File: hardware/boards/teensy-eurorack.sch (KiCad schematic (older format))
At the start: 101 parts, among them J1 Conn_01x08, J27 Conn_01x02, J28 Conn_02x08_Odd_Even, SW1 Rotary_Encoder_Switch, SW2 Rotary_Encoder_Switch, SW3 Rotary_Encoder_Switch, U1 CS42448, U2 AD5754BREZ, U3 AD5754BREZ, U4 Teensy4.1, U5 MCP1700-2502E_SOT23, U6 AD7606BSTZ, U7 6N138

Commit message: silkscreen
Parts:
- U5: value MCP1700-2502E_SOT23 -> MCP1700-2502E
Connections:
- net E1A: now also JB4.5 (Pin_5), JM4.5 (Pin_5); no longer JB4.7 (Pin_7), JM4.7 (Pin_7)
- net E1B: now also JB4.4 (Pin_4), JM4.4 (Pin_4); no longer JB4.6 (Pin_6), JM4.6 (Pin_6)
- net E2A: now also JB4.8 (Pin_8), JM4.8 (Pin_8); no longer JB4.5 (Pin_5), JM4.5 (Pin_5)
- net E2B: now also JB4.7 (Pin_7), JM4.7 (Pin_7); no longer JB4.4 (Pin_4), JM4.4 (Pin_4)
- net E3A: now also JB3.5 (Pin_5), JM3.5 (Pin_5); no longer JB4.3 (Pin_3), JM4.3 (Pin_3)
- net E3B: now also JB3.4 (Pin_4), JM3.4 (Pin_4); no longer JB4.2 (Pin_2), JM4.2 (Pin_2)
- net ES1: now also JB4.3 (Pin_3), JM4.3 (Pin_3); no longer JB3.3 (Pin_3), JM3.3 (Pin_3)
- net ES2: now also JB4.6 (Pin_6), JM4.6 (Pin_6); no longer JB3.2 (Pin_2), JM3.2 (Pin_2)
- net ES3: now also JB3.6 (Pin_6), JM3.6 (Pin_6); no longer JB4.8 (Pin_8), JM4.8 (Pin_8)
- net GND: now also JB3.7 (Pin_7), JM3.7 (Pin_7); no longer JB3.8 (Pin_8), JM3.8 (Pin_8)
- net P1: now also JB3.3 (Pin_3), JM3.3 (Pin_3); no longer JB3.7 (Pin_7), JM3.7 (Pin_7)
- net P2: now also JB3.2 (Pin_2), JM3.2 (Pin_2); no longer JB3.6 (Pin_6), JM3.6 (Pin_6)
- net P3: now also JB3.8 (Pin_8), JM3.8 (Pin_8); no longer JB3.5 (Pin_5), JM3.5 (Pin_5)
- net P4: now also JB4.2 (Pin_2), JM4.2 (Pin_2); no longer JB3.4 (Pin_4), JM3.4 (Pin_4)
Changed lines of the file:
@@
 P 13650 5950
 F 0 "U5" H 13500 5600 50  0000 L CNN
-F 1 "MCP1700-2502E_SOT23" H 12650 5700 50  0000 L CNN
+F 1 "MCP1700-2502E" H 12650 5700 50  0000 L CNN
 F 2 "Package_TO_SOT_SMD:SOT-23" H 13650 6175 50  0001 C CNN
 F 3 "http://ww1.microchip.com/downloads/en/DeviceDoc/20001826D.pdf" H 13650 5950 50  0001 C CNN
@@
 Wire Wire Line
 	14350 7350 14850 7350
+Text Label 14350 7150 0    49   ~ 0
+GND
+Text Label 14350 7550 0    49   ~ 0
+P1
+Text Label 14350 7650 0    49   ~ 0
+P2
 Text Label 14350 7050 0    49   ~ 0
-GND
-Text Label 14350 7150 0    49   ~ 0
-P1
-Text Label 14350 7250 0    49   ~ 0
-P2
-Text Label 14350 7350 0    49   ~ 0
 P3
 $Comp
@@
 Wire Wire Line
 	13100 7950 12150 7950
-Text Label 14350 7450 0    49   ~ 0
+Text Label 14500 9550 0    49   ~ 0
 P4
 Wire Wire Line
@@
 Wire Wire Line
 	14500 9650 15000 9650
-Text Label 14350 7550 0    49   ~ 0
+Text Label 14500 9450 0    49   ~ 0
 ES1
-Text Label 14350 7650 0    49   ~ 0
+Text Label 14500 9150 0    49   ~ 0
 ES2
+Text Label 14350 7250 0    49   ~ 0
+ES3
+Text Label 14500 9250 0    49   ~ 0
+E1A
+Text Label 14500 9350 0    49   ~ 0
+E1B
 Text Label 14500 8950 0    49   ~ 0
-ES3
+E2A
 Text Label 14500 9050 0    49   ~ 0
-E1A
-Text Label 14500 9150 0    49   ~ 0
-E1B
-Text Label 14500 9250 0    49   ~ 0
-E2A
-Text Label 14500 9350 0    49   ~ 0
 E2B
-Text Label 14500 9450 0    49   ~ 0
+Text Label 14350 7350 0    49   ~ 0
 E3A
-Text Label 14500 9550 0    49   ~ 0
+Text Label 14350 7450 0    49   ~ 0
 E3B
 $Comp

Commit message: silkscreen, corrections
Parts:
- added JBUSBA1, JBUSBB1: Conn_01x04, Connector_PinSocket_2.54mm:PinSocket_1x04_P2.54mm_Vertical, symbol Connector_Generic:Conn_01x04
- added JMUSBA1, JMUSBB1, JUSBA1, JUSBB1: Conn_01x04, Connector_PinHeader_2.54mm:PinHeader_1x04_P2.54mm_Vertical, symbol Connector_Generic:Conn_01x04
- added USBA1: USB-A-S-X-X-VT, footprints:USB-A-S-X-X-VT, symbol Connector_Generic:Conn_01x06
- added USBB1: 61400413321, footprints:WURTH_ELECTRONICS_61400413321_0, symbol Connector_Generic:Conn_01x06
- C12: value 4.7uF -> 4.7u
- C14: value 22uF -> 22u
- C16: value 100uF -> 100u
- C27, C29, C33, C34, C37: value 10uF -> 10u
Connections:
- net GND: now also JBUSBB1.1 (Pin_1), JMUSBB1.1 (Pin_1), JUSBB1.1 (Pin_1), USBB1.4 (Pin_4)
- new net: JBUSBA1.1 (Pin_1), JMUSBA1.1 (Pin_1), JUSBA1.1 (Pin_1), USBA1.4 (Pin_4)
- new net: JBUSBA1.2 (Pin_2), JMUSBA1.2 (Pin_2), JUSBA1.2 (Pin_2), USBA1.3 (Pin_3)
- new net: JBUSBA1.3 (Pin_3), JMUSBA1.3 (Pin_3), JUSBA1.3 (Pin_3), USBA1.2 (Pin_2)
- new net: JBUSBA1.4 (Pin_4), JMUSBA1.4 (Pin_4), JUSBA1.4 (Pin_4), USBA1.1 (Pin_1)
- new net: JBUSBB1.2 (Pin_2), JMUSBB1.2 (Pin_2), JUSBB1.2 (Pin_2), USBB1.3 (Pin_3)
- new net: JBUSBB1.3 (Pin_3), JMUSBB1.3 (Pin_3), JUSBB1.3 (Pin_3), USBB1.2 (Pin_2)
- new net: JBUSBB1.4 (Pin_4), JMUSBB1.4 (Pin_4), JUSBB1.4 (Pin_4), USBB1.1 (Pin_1)
- no-connect marks 32 -> 36
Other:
- moved on the sheet: JB1, JB2, JB3, JB4, JM1, JM2, JM3, JM4

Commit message: erc pass
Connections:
- net GND: now also U1.15 (DAC_SDIN3)
- no-connect marks 36 -> 63
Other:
- moved on the sheet: C42
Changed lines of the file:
@@
 L Device:C C42
 U 1 1 5EEE854A
-P 10200 7300
-F 0 "C42" V 10350 7300 50  0000 C CNN
-F 1 "10u" V 10050 7300 50  0000 C CNN
-F 2 "Capacitor_SMD:C_0805_2012Metric" H 10238 7150 50  0001 C CNN
-F 3 "~" H 10200 7300 50  0001 C CNN
-	1    10200 7300
+P 10800 7300
+F 0 "C42" V 10950 7300 50  0000 C CNN
+F 1 "10u" V 10650 7300 50  0000 C CNN
+F 2 "Capacitor_SMD:C_0805_2012Metric" H 10838 7150 50  0001 C CNN
+F 3 "~" H 10800 7300 50  0001 C CNN
+	1    10800 7300
 	0    1    1    0
 $EndComp
@@
 L power:GND #PWR0102
 U 1 1 5EEE9AAA
-P 10350 7300
-F 0 "#PWR0102" H 10350 7050 50  0001 C CNN
-F 1 "GND" H 10355 7127 50  0001 C CNN
-F 2 "" H 10350 7300 50  0001 C CNN
-F 3 "" H 10350 7300 50  0001 C CNN
-	1    10350 7300
+P 11100 7350
+F 0 "#PWR0102" H 11100 7100 50  0001 C CNN
+F 1 "GND" H 11105 7177 50  0001 C CNN
+F 2 "" H 11100 7350 50  0001 C CNN
+F 3 "" H 11100 7350 50  0001 C CNN
+	1    11100 7350
 	1    0    0    -1
 $EndComp
@@
 $EndComp
 NoConn ~ 14400 1650
-NoConn ~ 14350 1750
+NoConn ~ 14400 1750
 NoConn ~ 14400 4200
 NoConn ~ 14400 4300
@@
 F 3 "" H 12600 5950 50  0001 C CNN
 	1    12600 5950
-	0    -1   1    0
+	-1   0    0    -1
 $EndComp
 $Comp
@@
 	4850 6950 4950 6950
 Wire Wire Line
-	3150 5050 3150 5250
+	3150 5050 3150 5150
 Wire Wire Line
 	8250 6700 8250 6800
@@
 Wire Wire Line
 	14750 9150 14950 9150
+NoConn ~ 10150 3450
+NoConn ~ 10150 3250
+NoConn ~ 10150 2950
+NoConn ~ 10150 2850
+NoConn ~ 10150 2750
+NoConn ~ 7950 3450
+NoConn ~ 7950 3350
+NoConn ~ 7950 2550
+NoConn ~ 11750 7600
+NoConn ~ 11750 7500
+NoConn ~ 11750 7400
+NoConn ~ 12700 7400
+NoConn ~ 12700 7500
+NoConn ~ 12700 7600
+Connection ~ 3150 5150
+Wire Wire Line
+	3150 5150 3150 5250
+NoConn ~ 1300 11050
+NoConn ~ 2050 11050
+NoConn ~ 2800 11050
+NoConn ~ 3550 11050
+NoConn ~ 4350 11050
+NoConn ~ 5150 11050
+NoConn ~ 5950 11050
+NoConn ~ 6750 11050
+NoConn ~ 1150 9250
+NoConn ~ 1150 9150
+NoConn ~ 1650 9150
+NoConn ~ 1650 9250
+NoConn ~ 4250 8300
+Wire Wire Line
+	10050 7300 10650 7300
+Wire Wire Line
+	10950 7300 11100 7300
+Wire Wire Line
+	11100 7300 11100 7350
 $EndSCHEMATC

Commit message: split into two boards
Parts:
- removed C19, C20, C21, C22, C27, C29, C33, C34, C37, C42: 10u, Capacitor_SMD:C_0805_2012Metric, symbol Device:C
- removed C23, C24, C25, C26, C28, C30, C31, C32, C35, C36, C38, C39, C40, C41: 0.1u, Capacitor_SMD:C_0805_2012Metric, symbol Device:C
- removed C43, C44: 1u, Capacitor_SMD:C_0805_2012Metric, symbol Device:C
- removed D1: D, Diode_SMD:D_0805_2012Metric, symbol Device:D
- removed FPC_SD1: 1734592-8, footprints:HFW8R-1STE1LF, symbol Connector_Generic:Conn_01x10
- removed J1: Conn_01x08, footprints:ST7735, symbol Connector_Generic:Conn_01x08
- removed JB1, JB2: Conn_01x14, Connector_PinSocket_2.54mm:PinSocket_1x14_P2.54mm_Vertical, symbol Connector_Generic:Conn_01x14
- removed JB3, JB4: Conn_01x08, Connector_PinSocket_2.54mm:PinSocket_1x08_P2.54mm_Vertical, symbol Connector_Generic:Conn_01x08
- removed JBUSBA1, JBUSBB1: Conn_01x04, Connector_PinSocket_2.54mm:PinSocket_1x04_P2.54mm_Vertical, symbol Connector_Generic:Conn_01x04
- removed JIN1, JIN2, JIN3, JIN4, JIN5, JIN6, JIN7, JIN8, JOUT1, JOUT2, JOUT3, JOUT4, JOUT5, JOUT6, JOUT7, JOUT8: AudioJack2_SwitchT, footprints:WQP-PJ301M-12_JACK, symbol Connector:AudioJack2_SwitchT
- removed MIDI_IN1, MIDI_OUT1: DIN-5, footprints:OG-MIDI_SD-50BV, symbol Connector:DIN-5
- removed R36, R37, R38: 220, Resistor_SMD:R_0805_2012Metric, symbol Device:R
- removed R5, R6, R7: 4.7k, Resistor_SMD:R_0805_2012Metric, symbol Device:R
- removed RV1, RV2, RV3, RV4: R_POT, footprints:9MM_SNAP-IN_POT, symbol Device:R_POT
- removed SDCARD1: YAMAICHI_SD_CARD, footprints:YAMAICHI_MICROSD_VERTICAL, symbol Connector_Generic:Conn_01x10
- removed SW1, SW2, SW3: Rotary_Encoder_Switch, Rotary_Encoder:RotaryEncoder_Alps_EC12E-Switch_Vertical_H20mm_CircularMountingHoles, symbol Device:Rotary_Encoder_Switch
- removed U2, U3: AD5754BREZ, Package_SO:HTSSOP-24-1EP_4.4x7.8mm_P0.65mm_EP3.2x5mm, symbol teensy-eurorack:AD5754BREZ
- removed U5: MCP1700-2502E, Package_TO_SOT_SMD:SOT-23, symbol Regulator_Linear:MCP1700-2502E_SOT23
- removed U6: AD7606BSTZ, Package_QFP:LQFP-64_10x10mm_P0.5mm, symbol teensy-eurorack:AD7606BSTZ
- removed U7: 6N138, footprints:6N138S, symbol Isolator:6N138
- removed USBA1: USB-A-S-X-X-VT, footprints:USB-A-S-X-X-VT, symbol Connector_Generic:Conn_01x06
- removed USBB1: 61400413321, footprints:WURTH_ELECTRONICS_61400413321_0, symbol Connector_Generic:Conn_01x06
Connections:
- net labels removed: DAC_REF2V5, VGND1, VGND2, VGND3, VGND4, VGND5, VGND6, VGND7, VGND8, VIN1, VIN2, VIN3, VIN4, VIN5, VIN6, VIN7, VIN8, VOUT1, VOUT2, VOUT3, VOUT4, VOUT5, VOUT6, VOUT7, VOUT8
- wire segments 288 -> 145
- no-connect marks 63 -> 34
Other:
- note removed: "ADC"
- note removed: "DAC"
- note removed: "ST3375 TFT"

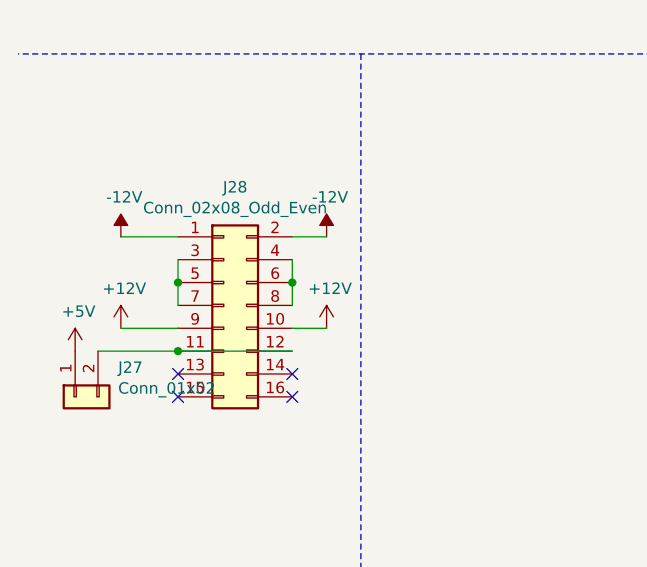
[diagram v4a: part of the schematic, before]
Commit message: mainboard passes drc
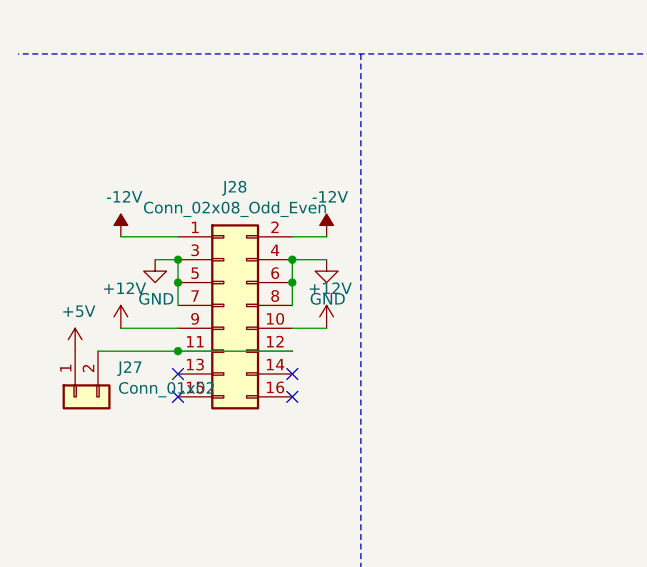
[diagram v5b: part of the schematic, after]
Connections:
- wire segments 145 -> 147
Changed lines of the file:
@@
 Wire Wire Line
 	11750 6900 13100 6900
+$Comp
+L power:GND #PWR?
+U 1 1 5F061C98
+P 1050 8650
+F 0 "#PWR?" H 1050 8400 50  0001 C CNN
+F 1 "GND" H 1055 8477 50  0000 C CNN
+F 2 "" H 1050 8650 50  0001 C CNN
+F 3 "" H 1050 8650 50  0001 C CNN
+	1    1050 8650
+	1    0    0    -1
+$EndComp
+$Comp
+L power:GND #PWR?
+U 1 1 5F0623CA
+P 1800 8650
+F 0 "#PWR?" H 1800 8400 50  0001 C CNN
+F 1 "GND" H 1805 8477 50  0000 C CNN
+F 2 "" H 1800 8650 50  0001 C CNN
+F 3 "" H 1800 8650 50  0001 C CNN
+	1    1800 8650
+	1    0    0    -1
+$EndComp
+Wire Wire Line
+	1050 8650 1150 8650
+Connection ~ 1150 8650
+Wire Wire Line
+	1800 8650 1650 8650
+Connection ~ 1650 8650
 $EndSCHEMATC

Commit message: changed schematic from A3 to A4
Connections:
- wire segments 147 -> 146
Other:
- note removed: "PIN HEADERS"
- moved on the sheet: C1, C10, C11, C12, C13, C14, C15, C16, C17, C18, C2, C3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

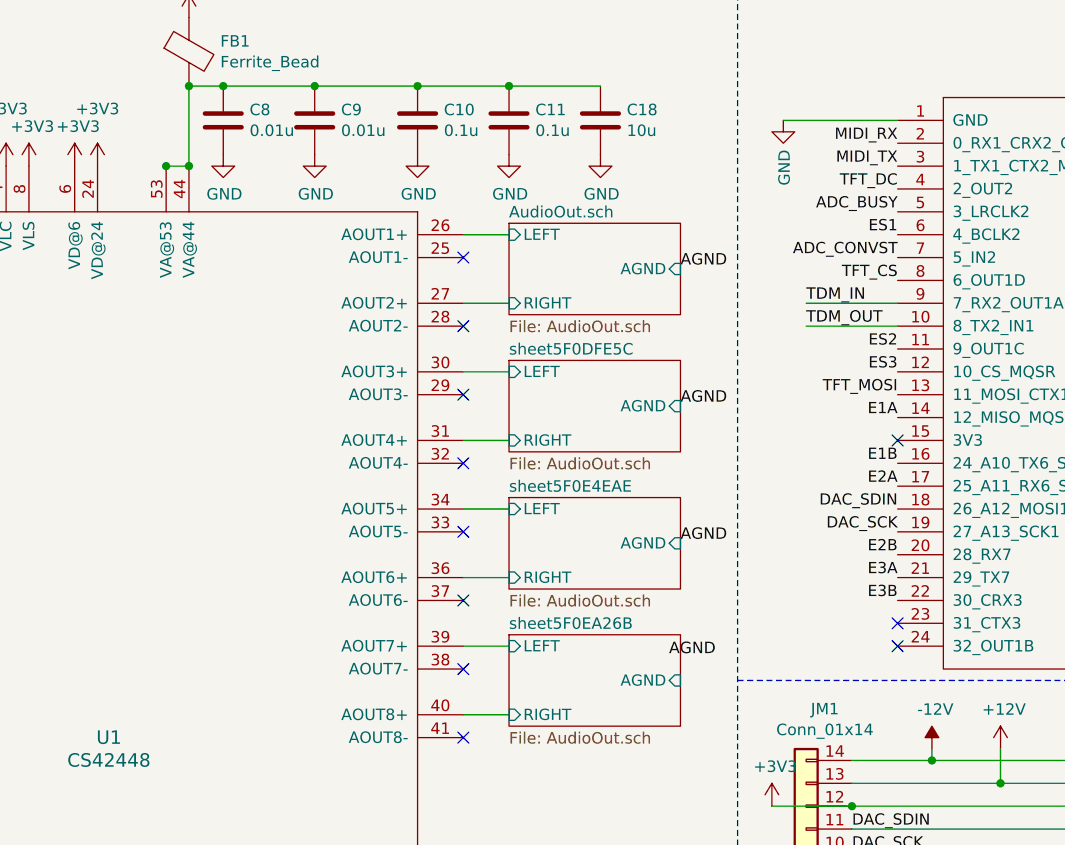
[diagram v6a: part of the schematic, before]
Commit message: connected DAC_SCK output (pin 19) to pin 31, corrected audio out 4 AGND net (was disconnected)
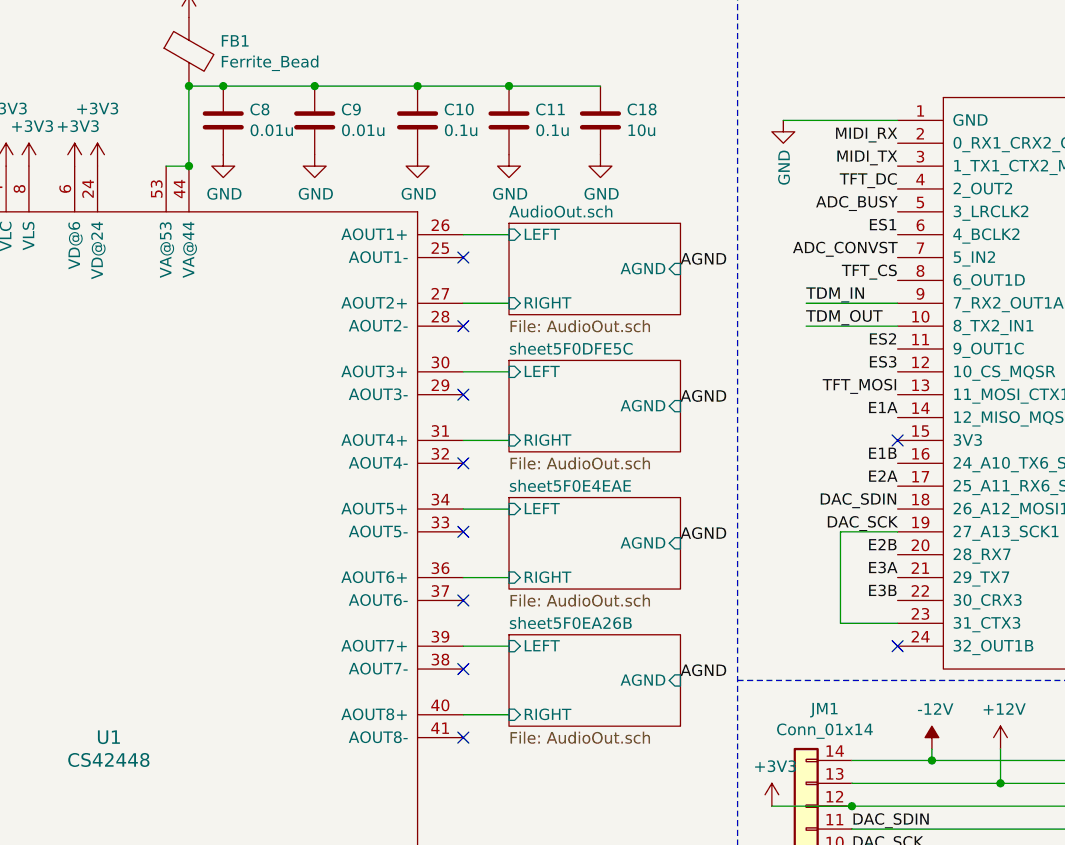
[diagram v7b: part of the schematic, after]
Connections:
- wire segments 146 -> 149
- no-connect marks 34 -> 33
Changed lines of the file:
@@
 Text Label 7000 2900 0    50   ~ 0
 AGND
-Text Label 6950 3400 0    50   ~ 0
+Text Label 7000 3500 0    50   ~ 0
 AGND
 Text Notes 7250 400  2    98   ~ 0
@@
 NoConn ~ 10150 2650
 NoConn ~ 7950 3350
-NoConn ~ 7950 3250
 NoConn ~ 7950 2450
 Connection ~ 3050 4650
@@
 Wire Notes Line
 	7250 3500 11200 3500
-Connection ~ 4750 1250
+Wire Wire Line
+	7950 3250 7700 3250
+Wire Wire Line
+	7700 3250 7700 2850
+Wire Wire Line
+	7700 2850 7950 2850
 $EndSCHEMATC
